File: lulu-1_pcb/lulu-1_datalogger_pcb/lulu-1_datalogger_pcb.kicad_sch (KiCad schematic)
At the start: 37 parts, among them J1 SD_Card_Receptacle, J3 USB_C_Receptacle_USB2.0_16P, J4 Conn_01x20_Socket, J5 Screw_Terminal_01x03, SW1 SW_Nidec_CAS-120A1, U1 STM32F401RETx, U2 BMP280, U3 MPU-6050, U4 W25Q16JVSS, U5 BD33FC0FP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

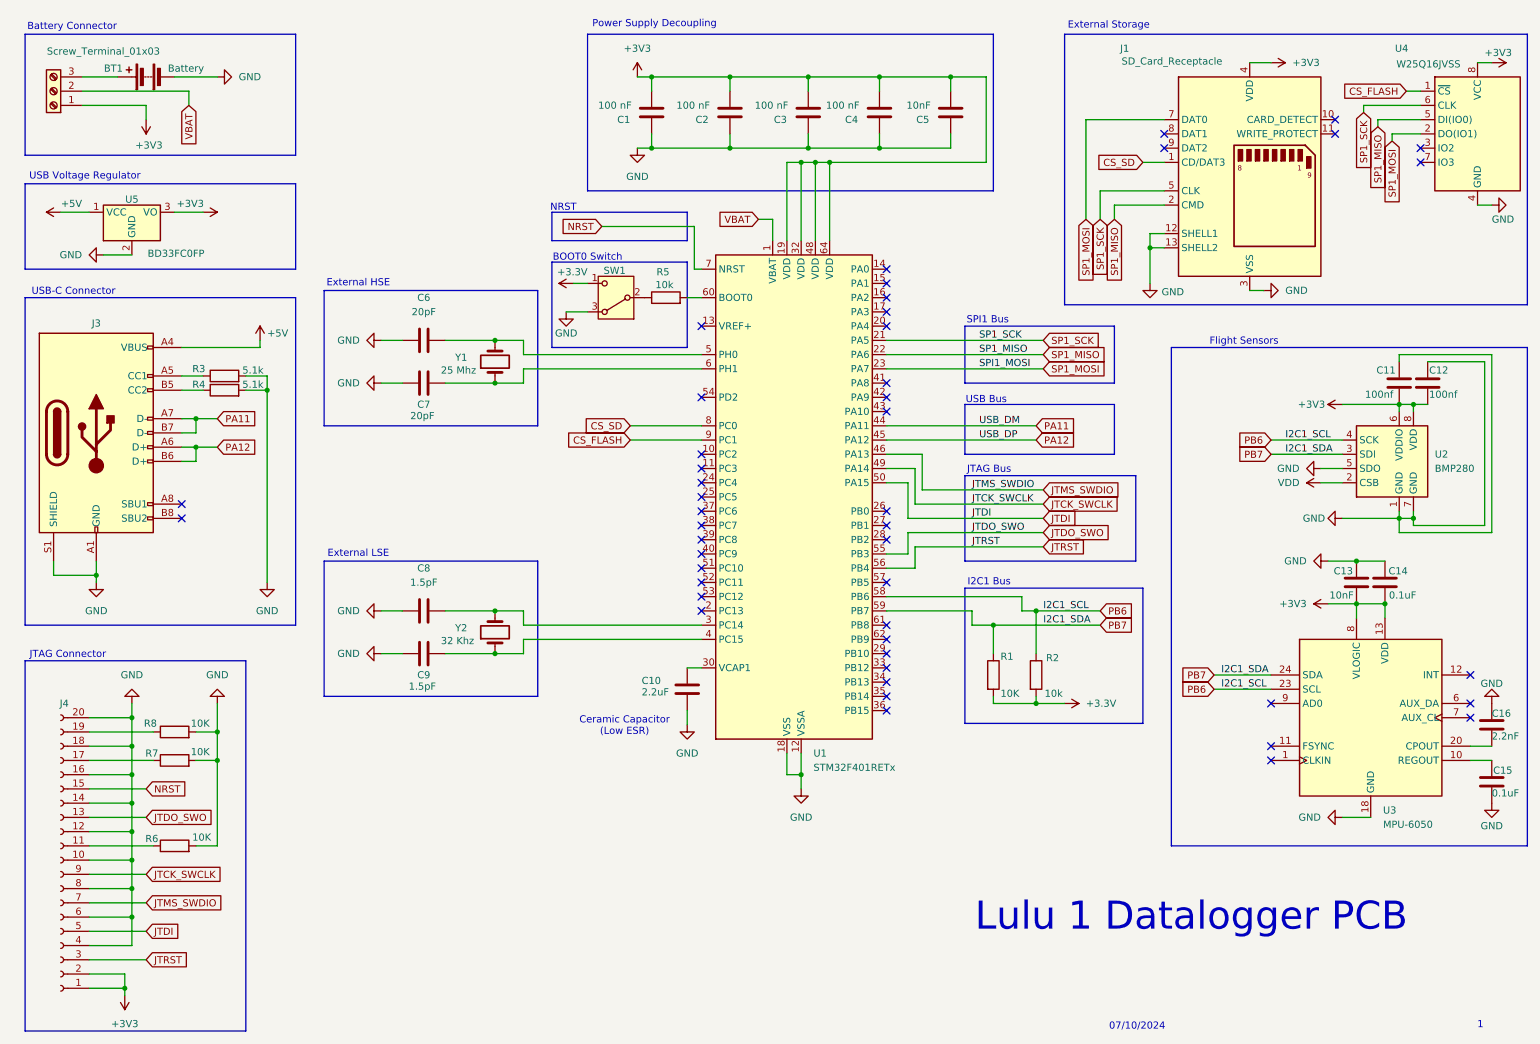
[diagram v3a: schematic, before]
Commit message: changed MOSI and MISO connection for flash chiP
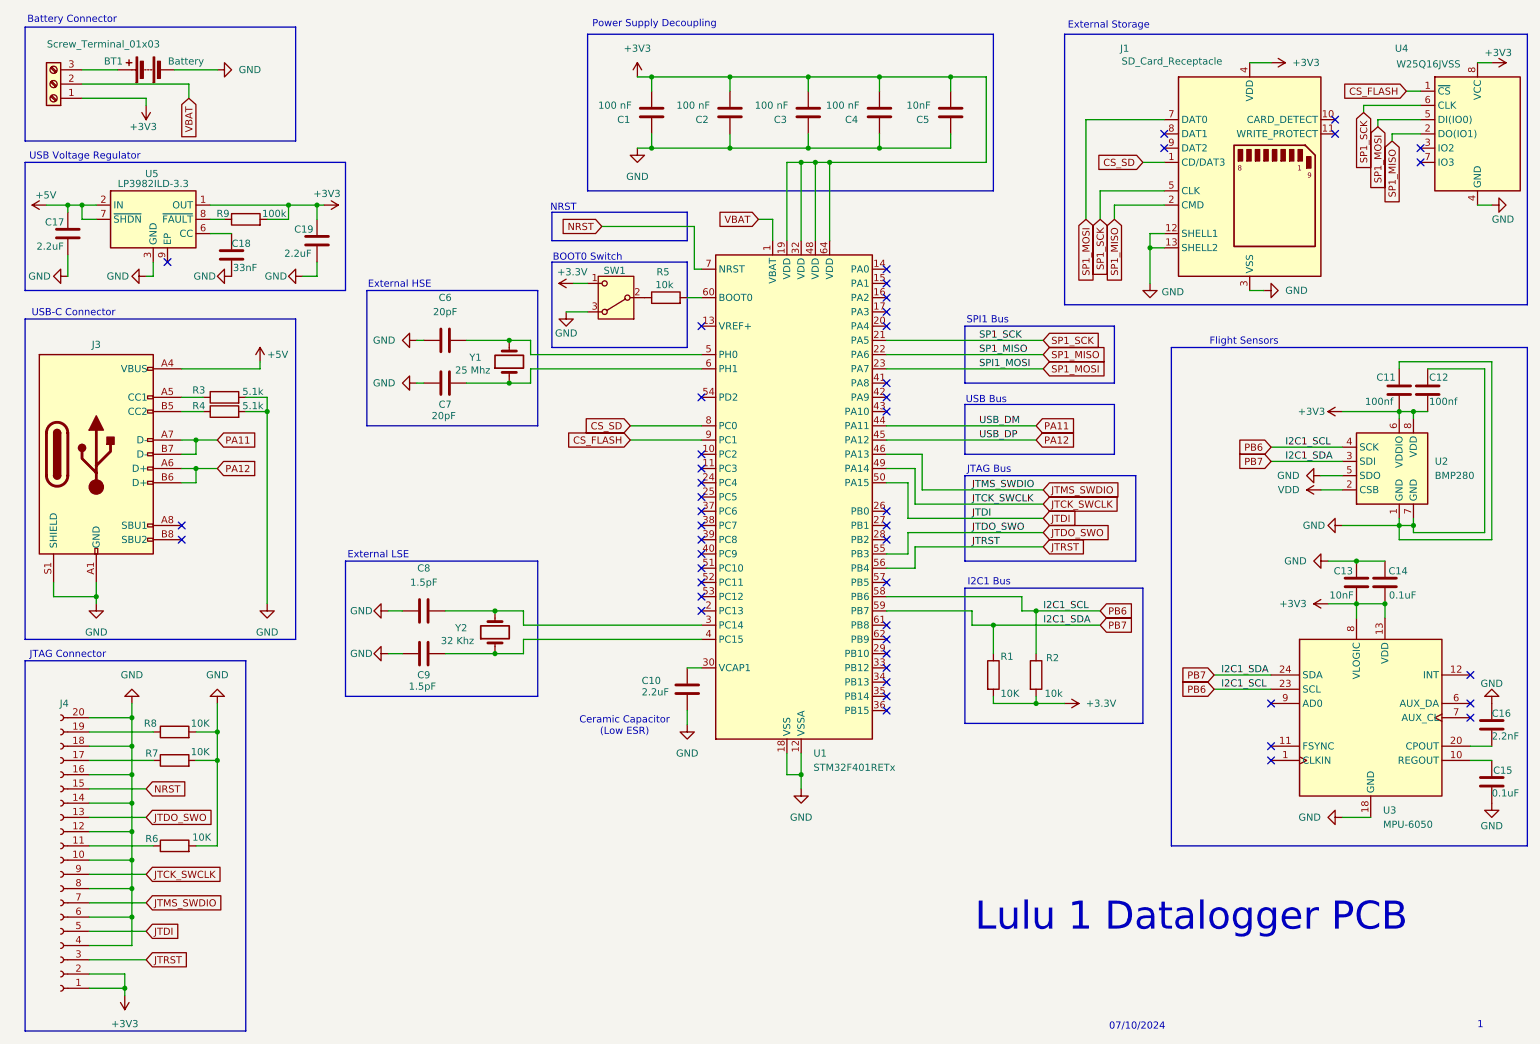
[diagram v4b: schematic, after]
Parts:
- removed U5: BD33FC0FP, Package_TO_SOT_SMD:TO-252-2, symbol Regulator_Linear:BD33FC0FP
- added C17, C19: 2.2uF, symbol Device:C
- added C18: 33nF, symbol Device:C
- added R9: 100k, symbol Device:R
- added U5: LP3982ILD-3.3, Package_SON:WSON-8-1EP_3x2.5mm_P0.5mm_EP1.2x1.5mm_PullBack_ThermalVias, symbol Regulator_Linear:LP3982ILD-3.3
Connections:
- net +3V3: now also C19.1, R9.2, U5.1 (OUT), U5.4 (OUT)
- net +5V: now also C17.1, U5.2 (IN), U5.7 (~{SHDN})
- net GND: now also C17.2, C18.2, C19.2, U5.3 (GND)
- net SP1_MISO: now also U4.2 (DO(IO1)); no longer U4.5 (DI(IO0))
- net SP1_MOSI: now also U4.5 (DI(IO0)); no longer U4.2 (DO(IO1))
- new net: C18.1, U5.6 (CC)
- new net: R9.1, U5.8 (~{FAULT})
- no-connect marks 47 -> 48
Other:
- moved on the sheet: BT1, C11, C12, C6, C7, J3, R3, R4, U2, Y1

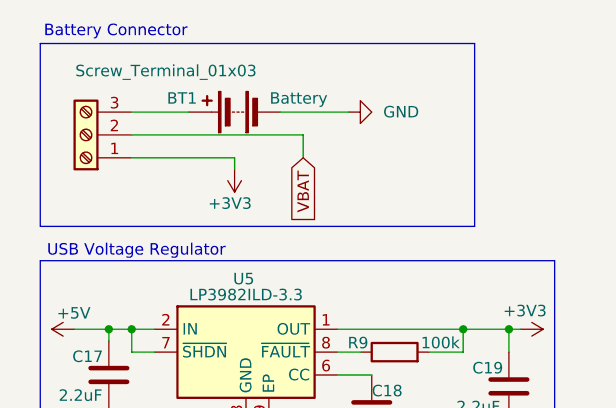
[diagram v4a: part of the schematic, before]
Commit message: added 0805 footprints for resistors and capacitors
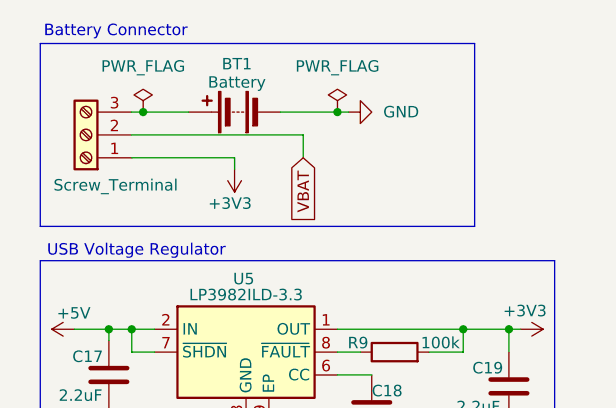
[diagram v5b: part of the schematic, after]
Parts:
- C1, C10, C11, C12, C13, C14, C15, C16, C17, C18, C19, C2, C3, C4, C5, C6, C7, C8, C9: footprint (none) -> Capacitor_SMD:C_0805_2012Metric
- J5: value Screw_Terminal_01x03 -> Screw_Terminal
- R1, R2, R3, R4, R5, R6, R7, R8, R9: footprint (none) -> Resistor_SMD:R_0805_2012Metric

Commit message: updated openrocket values for avionics
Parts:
- J1: footprint (none) -> Connector_Card:SD-SIM_microSD-microSIM_Molex_104168-1620
- J3: footprint (none) -> Connector_USB:USB_C_Receptacle_Amphenol_12401548E4-2A
- J4: footprint (none) -> Connector:FanPinHeader_1x04_P2.54mm_Vertical
- J5: footprint (none) -> TerminalBlock:TerminalBlock_Altech_AK300-3_P5.00mm
- Y1, Y2: footprint (none) -> Crystal:Crystal_AT310_D3.0mm_L10.0mm_Horizontal
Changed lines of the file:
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@@
 			)
 		)
-		(property "Footprint" ""
+		(property "Footprint" "Crystal:Crystal_AT310_D3.0mm_L10.0mm_Horizontal"
 			(at 99.06 123.19 0)
 			(effects
@@
 			)
 		)
-		(property "Footprint" ""
+		(property "Footprint" "TerminalBlock:TerminalBlock_Altech_AK300-3_P5.00mm"
 			(at 20.32 25.4 0)
 			(effects
@@
 			)
 		)
-		(property "Footprint" ""
+		(property "Footprint" "Connector_Card:SD-SIM_microSD-microSIM_Molex_104168-1620"
 			(at 242.57 45.212 0)
 			(effects
@@
 			)
 		)
-		(property "Footprint" ""
+		(property "Footprint" "Connector:FanPinHeader_1x04_P2.54mm_Vertical"
 			(at 21.59 163.83 0)
 			(effects
@@
 			)
 		)
-		(property "Footprint" ""
+		(property "Footprint" "Crystal:Crystal_AT310_D3.0mm_L10.0mm_Horizontal"
 			(at 101.6 74.93 0)
 			(effects
@@
 			)
 		)
-		(property "Footprint" ""
+		(property "Footprint" "Connector_USB:USB_C_Receptacle_Amphenol_12401548E4-2A"
 			(at 31.75 91.44 0)
 			(effects

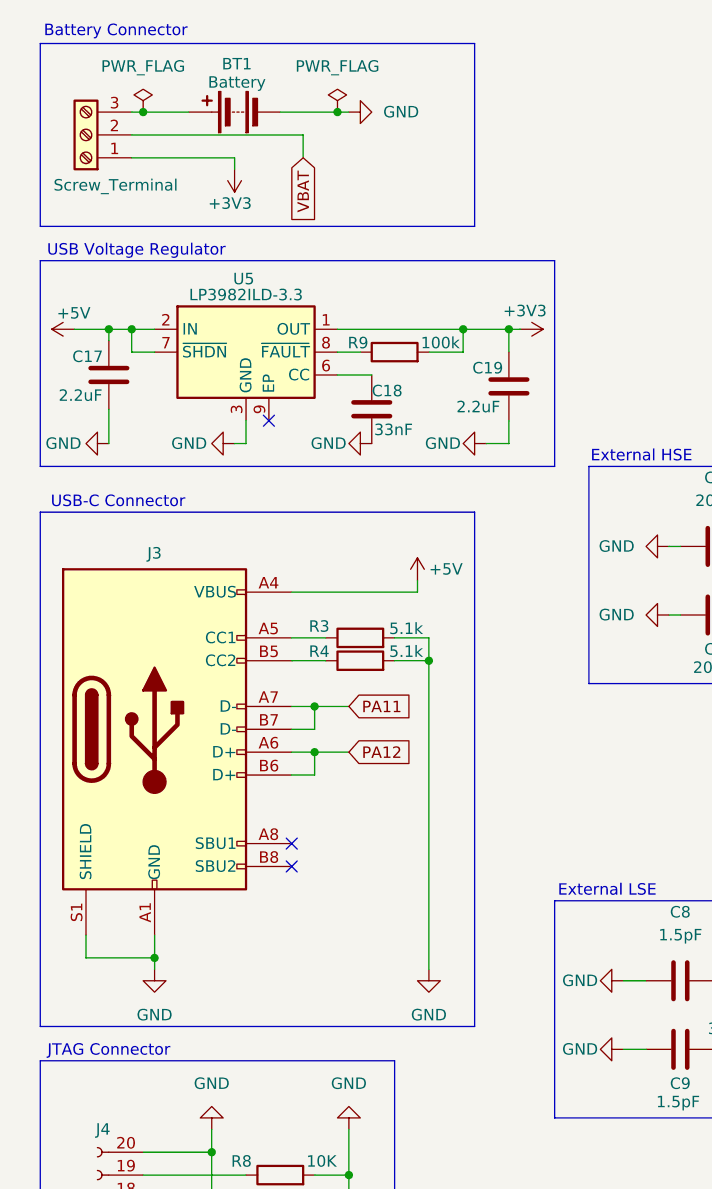
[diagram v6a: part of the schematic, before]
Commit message: Replaced footprint and symbol for USB with part that i am ordering
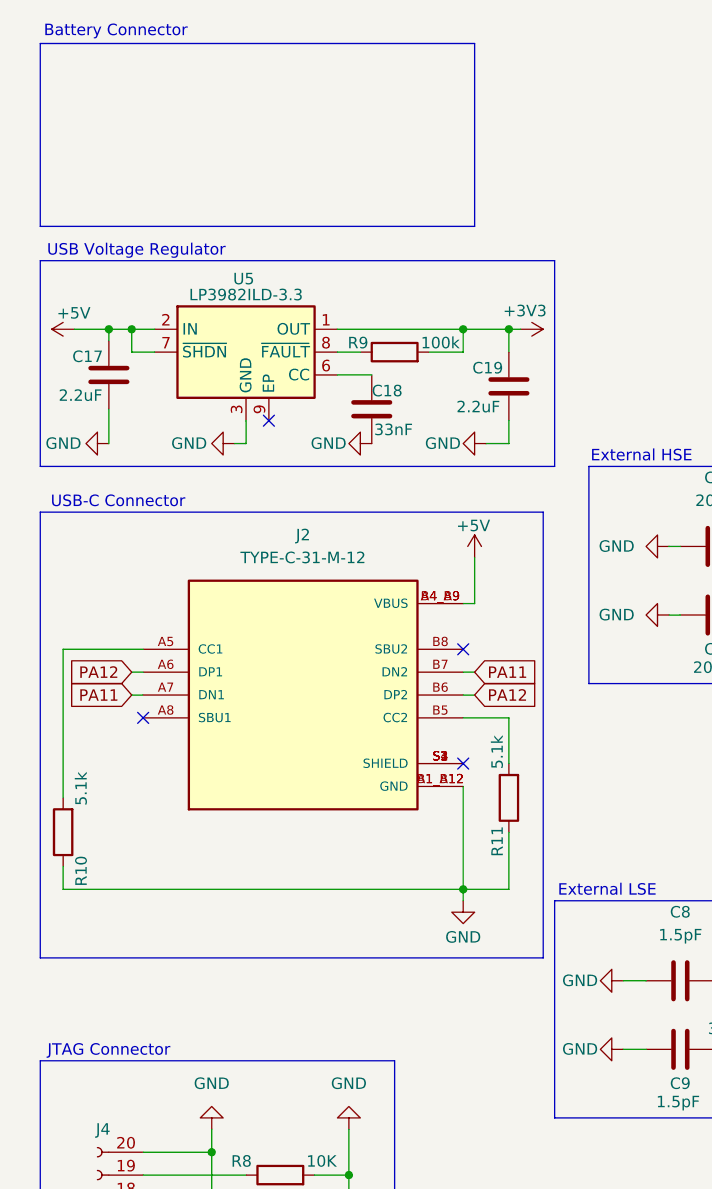
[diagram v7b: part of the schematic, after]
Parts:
- removed BT1: Battery, symbol Device:Battery
- removed J3: USB_C_Receptacle_USB2.0_16P, Connector_USB:USB_C_Receptacle_Amphenol_12401548E4-2A, symbol Connector:USB_C_Receptacle_USB2.0_16P
- removed J5: Screw_Terminal, TerminalBlock:TerminalBlock_Altech_AK300-3_P5.00mm, symbol Connector:Screw_Terminal_01x03
- removed R3, R4: 5.1k, Resistor_SMD:R_0805_2012Metric, symbol Device:R
- added J2: TYPE-C-31-M-12, TYPE-C-31-M-12:HRO_TYPE-C-31-M-12, symbol TYPE-C-31-M-12:TYPE-C-31-M-12
- added R10, R11: 5.1k, Resistor_SMD:R_0805_2012Metric, symbol Device:R
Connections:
- net +5V: now also J2.A4_B9 (VBUS), J2.B4_A9 (VBUS)
- net GND: now also J2.A1_B12 (GND), J2.B1_A12 (GND), R10.1, R11.1
- net PA11: now also J2.A7 (DN1), J2.B7 (DN2)
- net PA12: now also J2.A6 (DP1), J2.B6 (DP2)
- new net: J2.A5 (CC1), R10.2
- new net: J2.B5 (CC2), R11.2
- new net: J2.S1 (SHIELD), J2.S2 (SHIELD), J2.S3 (SHIELD), J2.S4 (SHIELD)
- no-connect marks 48 -> 49

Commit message: tidy circuit
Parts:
- added J3: Conn_01x02_Pin, symbol Connector:Conn_01x02_Pin
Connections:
- net +3V3: now also J3.1 (Pin_1)
- net GND: now also J3.2 (Pin_2); no longer J1.12 (SHELL1), J1.13 (SHELL2)
- no-connect marks 49 -> 51
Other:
- moved on the sheet: C11, C12, C13, C14, C17, C18, C19, C6, C7, C8, C9, J1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
